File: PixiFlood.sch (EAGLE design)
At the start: 37 parts, among them IC1 TC7W04FP-0.65, IC2 WS2811S, IC3 78L05Z, U1 PT4115B89E, U2 PT4115B89E, U3 PT4115B89E, X1 22-23-2031, X2 22-23-2031

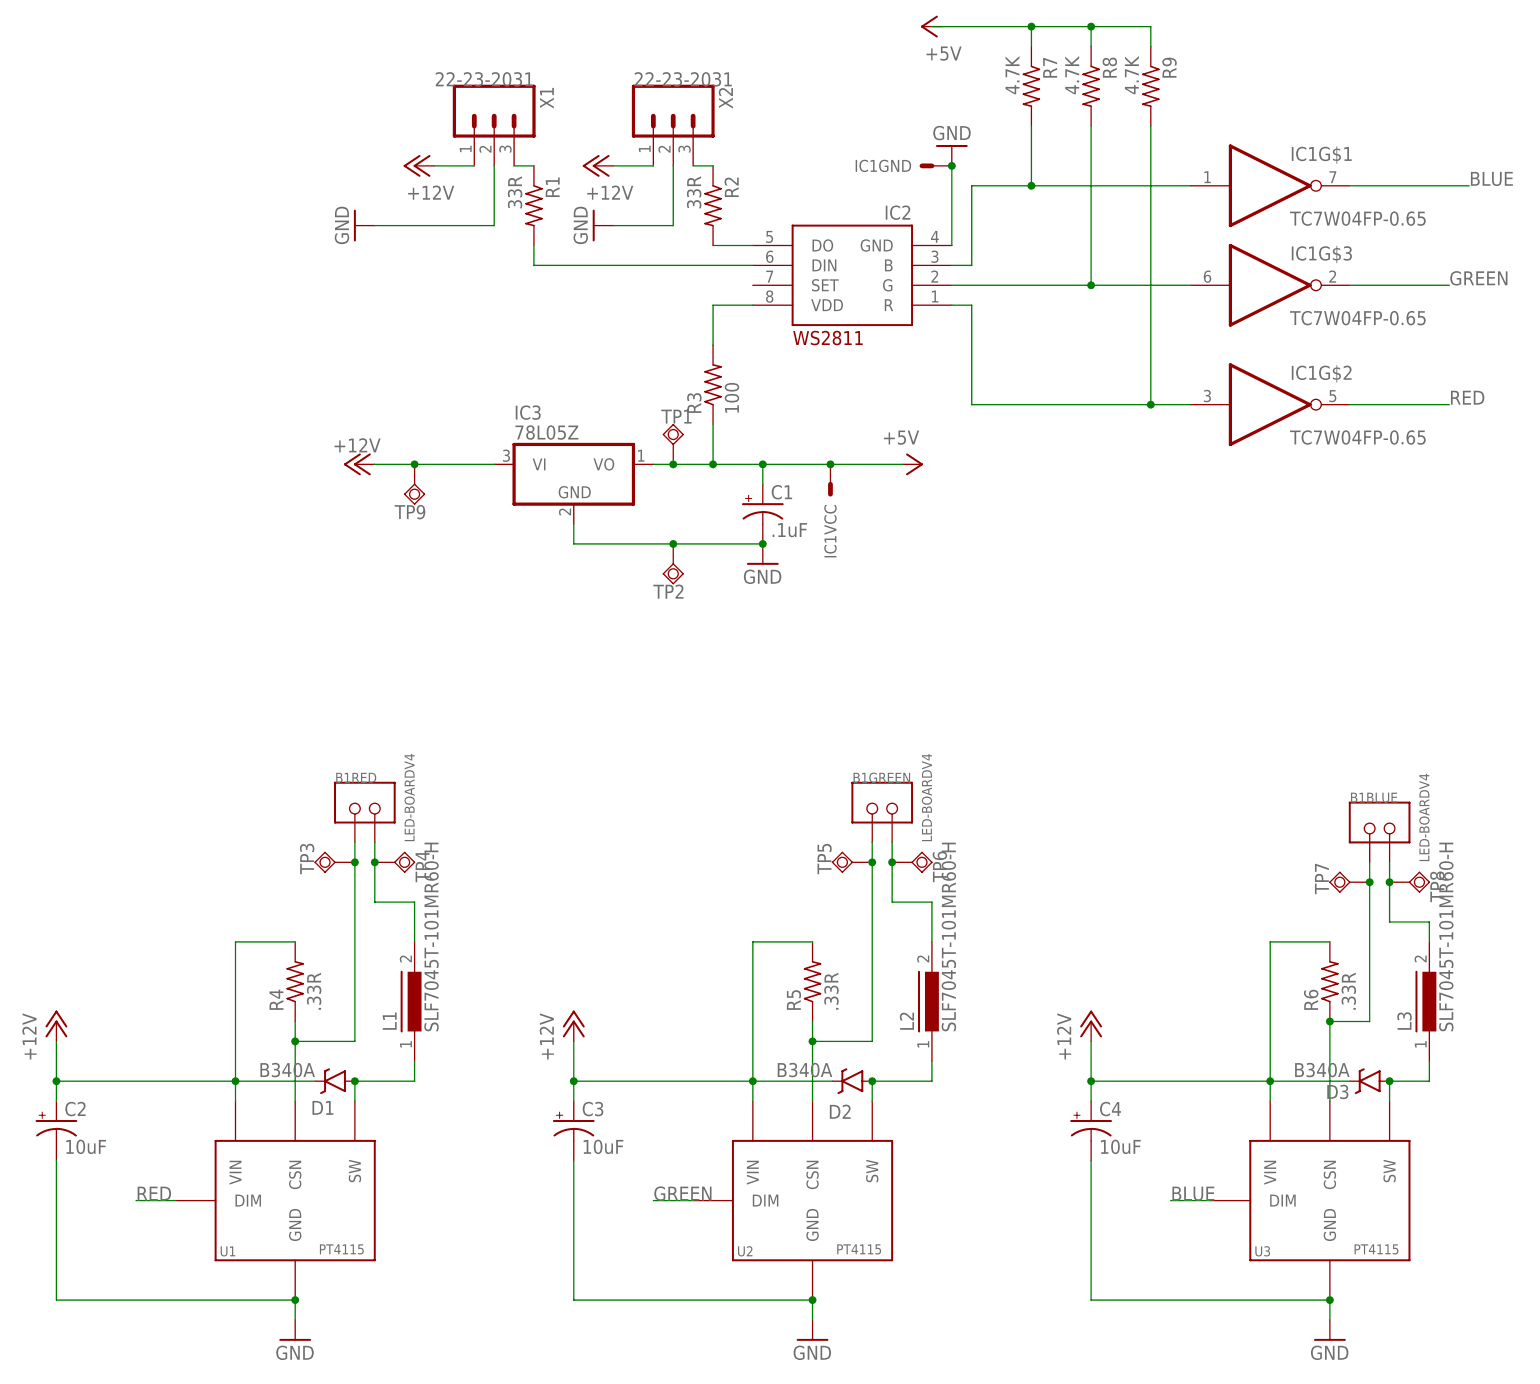
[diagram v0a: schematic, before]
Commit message: Reworked layout
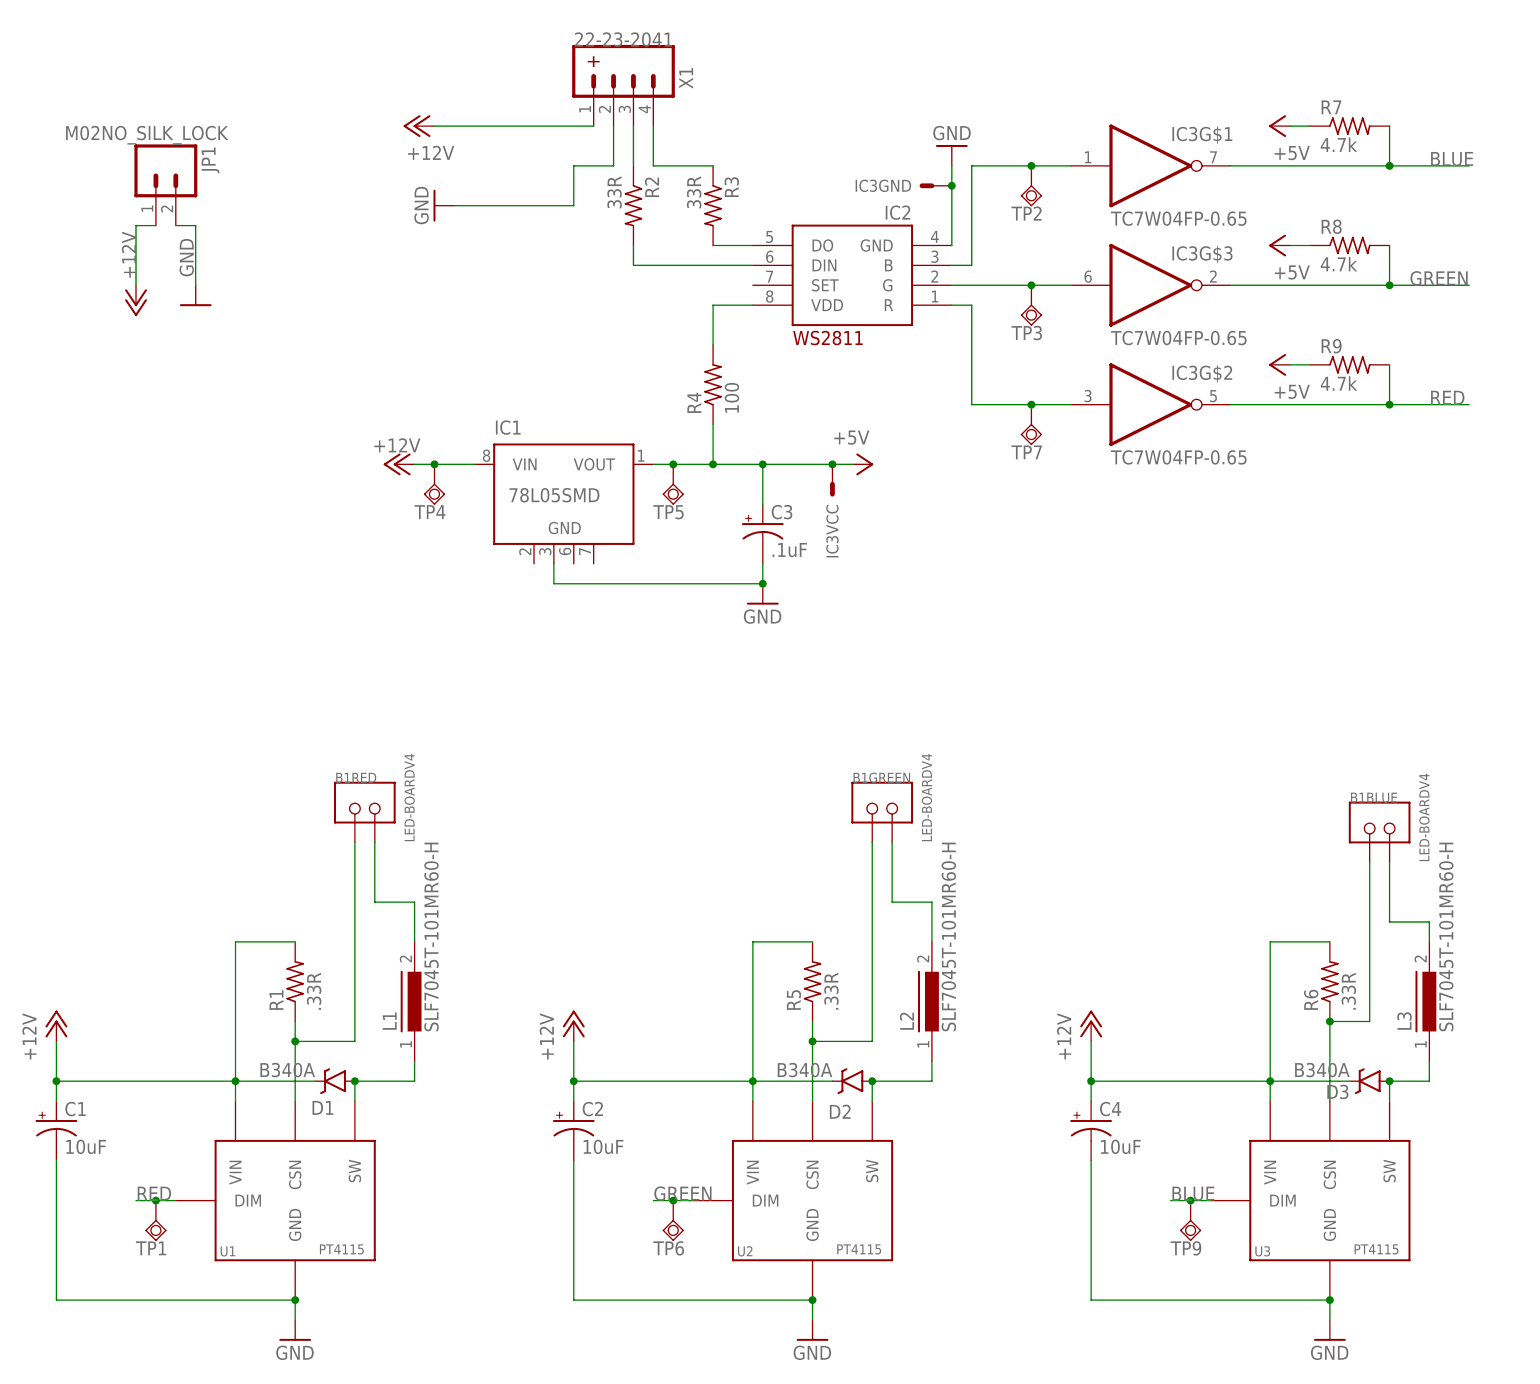
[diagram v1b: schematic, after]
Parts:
- removed TP8: TPSQTP15SQ, testpad:TPSQTP15SQ
- removed X2: 22-23-2031, MyLibrary:22-23-2031
- added JP1: M02NO_SILK_LOCK, connectors:M02NO_SILK_LOCK
- C1: value .1uF -> 10uF; device capacitors:CAP_POL1206 -> capacitors:CAP_POLCASE-D
- C3: value 10uF -> .1uF; device capacitors:CAP_POLCASE-D -> capacitors:CAP_POL1206
- IC1: value TC7W04FP-0.65 -> 78L05SMD; device logic:TC7W04FP-0.65 -> regulators:78L05SMD
- IC3: value 78L05Z -> TC7W04FP-0.65; device linear:78L05Z -> logic:TC7W04FP-0.65
- R1: value 33R -> .33R; device rcl:R-US_R1206 -> resistor:R-US_R1210
- R3: value 100 -> 33R
- R4: value .33R -> 100; device resistor:R-US_R1210 -> rcl:R-US_R1206
- R7, R8, R9: value 4.7K -> 4.7k; device rcl:R-US_R0805 -> rcl:R-US_R1206
- TP1: value TPSQTP20R -> TPSQTP15R; device testpad:TPSQTP20R -> testpad:TPSQTP15R
- TP2: value TPSQTP20SQ -> TPSQTP15R; device testpad:TPSQTP20SQ -> testpad:TPSQTP15R
- TP4, TP6: value TPSQTP15SQ -> TPSQTP15R; device testpad:TPSQTP15SQ -> testpad:TPSQTP15R
- U1, U2, U3: value PT4115B89E -> PT4115B89E-A; device drivers:PT4115B89E -> drivers:PT4115B89E-A
- X1: value 22-23-2031 -> 22-23-2041; device MyLibrary:22-23-2031 -> connectors:22-23-2041
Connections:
- removed net N$18: R7.1, R8.1, R9.1
- net +12V: now also C1.+, IC1G$1.VIN, JP1.1, R1.2, TP4.TP; no longer C3.+, IC3.VI, R4.2, TP9.TP, X2.1
- net +5V: now also C3.+, IC1G$1.VOUT, IC3VCC.S, R4.1, R7.1, R8.1, R9.1, TP5.TP; no longer C1.+, IC1VCC.S, IC3.VO, R3.1, TP1.TP
- net BLUE: now also IC3G$1.O, R7.2, TP9.TP; no longer IC1G$1.O
- net BOUT: no longer TP7.TP
- net GND: now also IC1G$1.GND@2, IC3GND.S, JP1.2; no longer IC1GND.S, IC3.GND, TP2.TP, X2.2
- net GOUT: no longer TP5.TP
- net GREEN: now also IC3G$3.O, R8.2, TP6.TP; no longer IC1G$3.O
- net N$10: no longer TP8.TP
- net N$14: now also R4.2; no longer R3.2
- net N$15: now also IC3G$2.I, TP7.TP; no longer IC1G$2.I, R9.2
- net N$16: now also IC3G$1.I, TP2.TP; no longer IC1G$1.I, R7.2
- net N$19: now also IC3G$3.I, TP3.TP; no longer IC1G$3.I, R8.2
- net N$3: no longer TP4.TP
- net N$4: now also R3.1, X1.4; no longer R2.1, X2.3
- net N$6: now also R2.1; no longer R1.1
- net N$7: now also R3.2; no longer R2.2
- net N$8: now also R2.2; no longer R1.2
- net N$9: no longer TP6.TP
- net RED: now also IC3G$2.O, R9.2, TP1.TP; no longer IC1G$2.O
- net ROUT: now also R1.1; no longer R4.1, TP3.TP
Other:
- moved on the sheet: C1, C2, C3, R1, R2, R3, R4, R7, R8, R9, TP1, TP2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

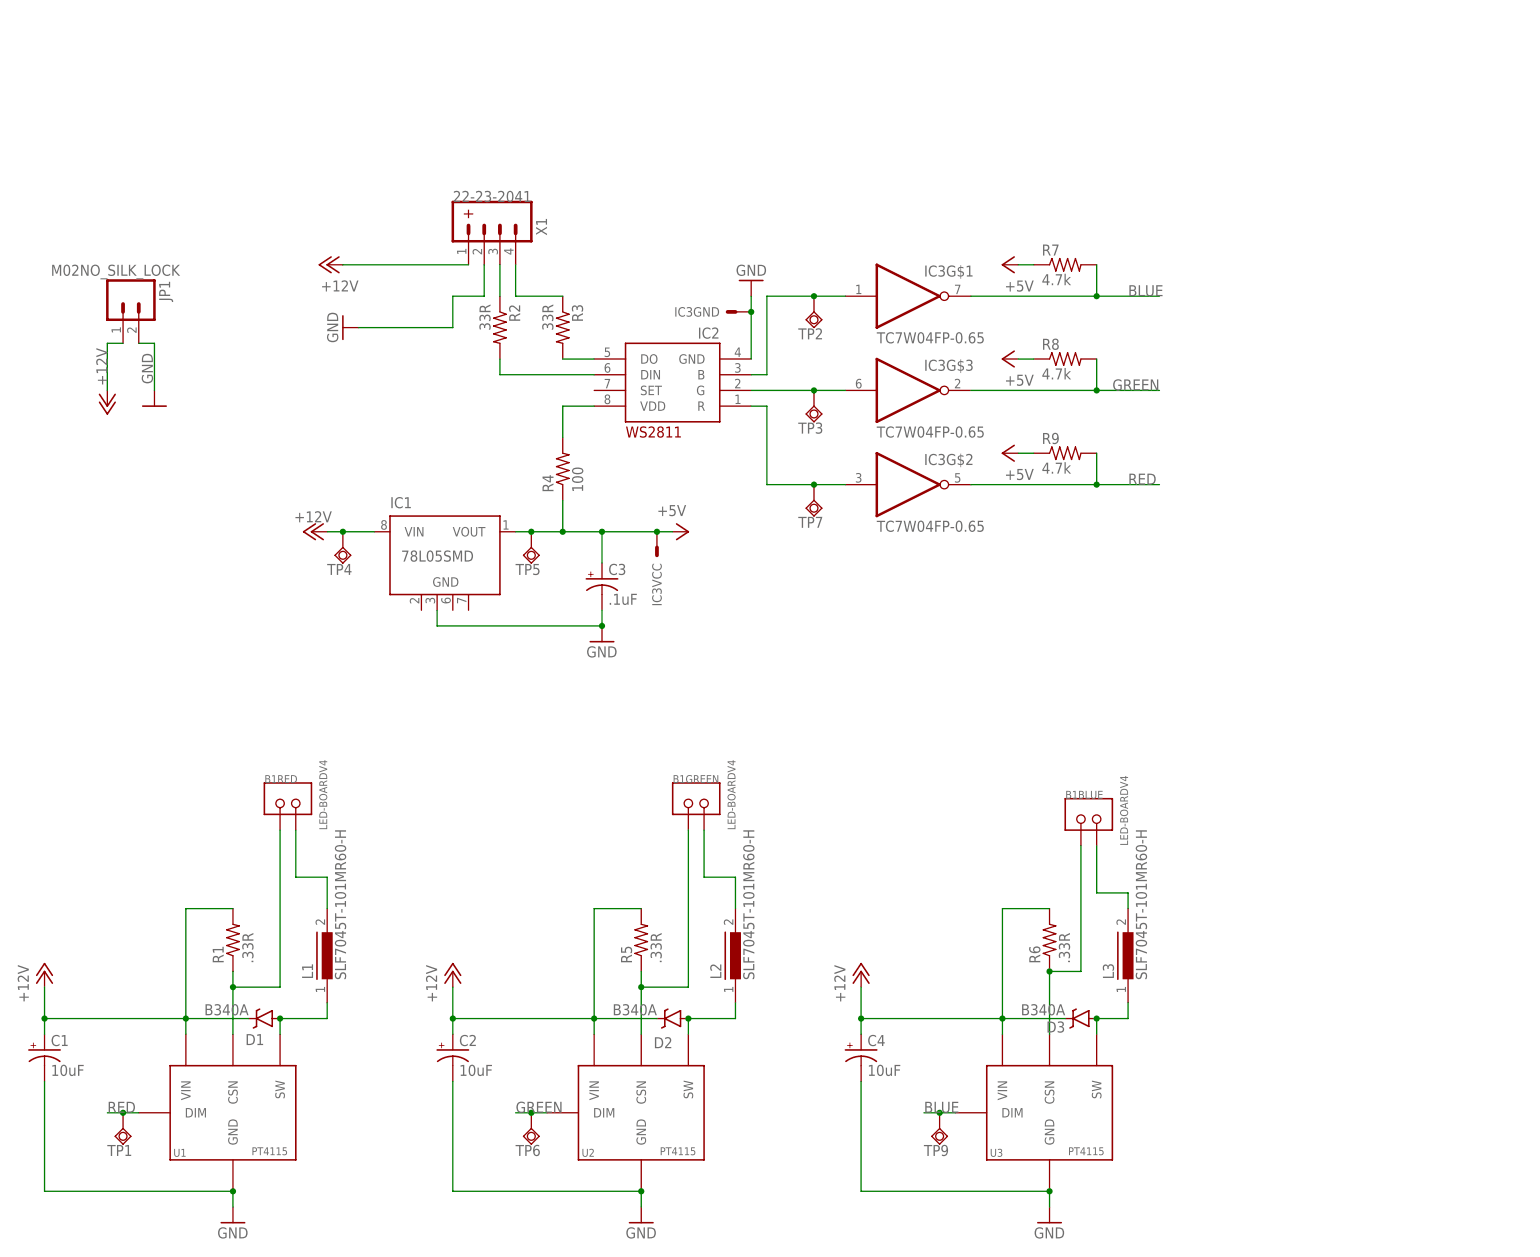
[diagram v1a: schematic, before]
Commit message: Reworked layout
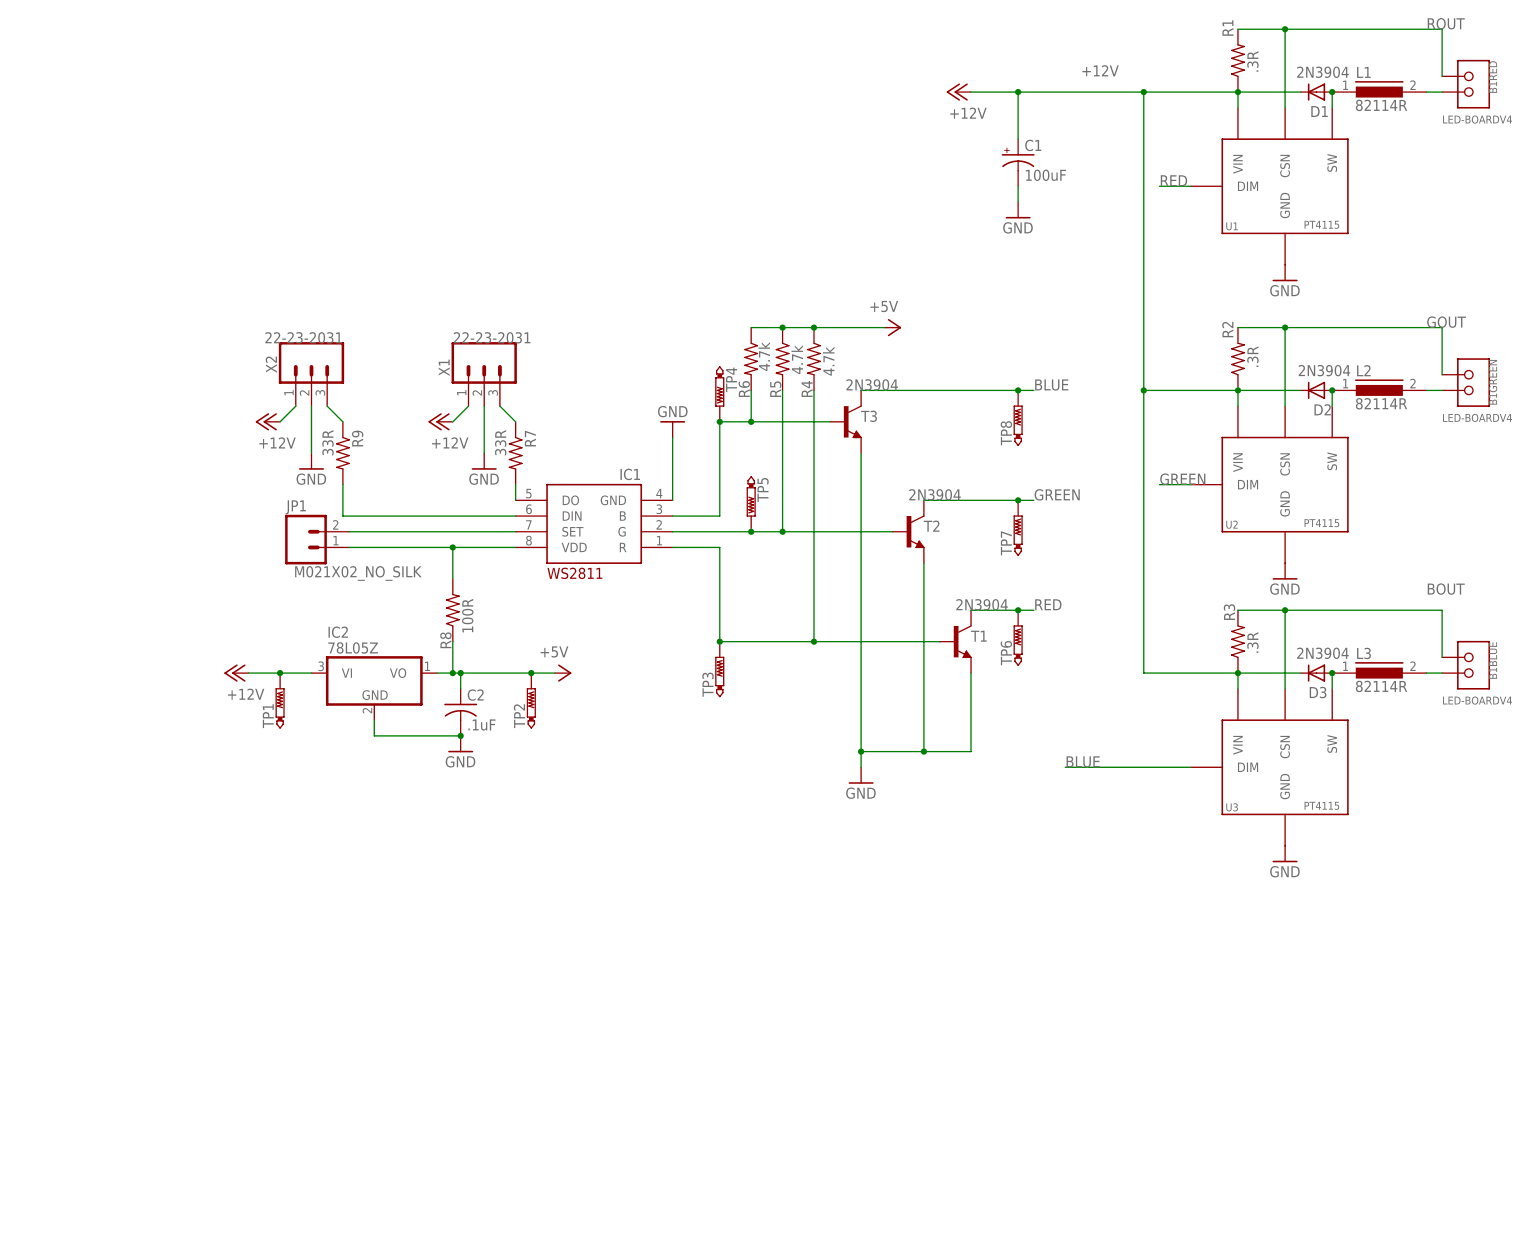
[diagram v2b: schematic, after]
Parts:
- removed C3: .1uF, capacitors:CAP_POL1206
- removed C4: 10uF, capacitors:CAP_POLCASE-D
- removed IC3: TC7W04FP-0.65, logic:TC7W04FP-0.65
- removed TP9: TPSQTP15R, testpad:TPSQTP15R
- added T1, T2, T3: 2N3904, transistor:2N3904
- added TP8: PTR1B1,27, testpad:PTR1B1,27
- added X2: 22-23-2031, connectors:22-23-2031
- C1: value 10uF -> 100uF; device capacitors:CAP_POLCASE-D -> rcl:CPOL-USTT2D6L
- C2: value 10uF -> .1uF; device capacitors:CAP_POLCASE-D -> rcl:C-US050-024X044
- D1, D2, D3: value B340A -> 2N3904; device SparkFun-DiscreteSemi:DIODE-SCHOTTKY-B340A -> diode:DIODE-DO07
- IC1: value 78L05SMD -> WS2811-SOP8; device regulators:78L05SMD -> MyLibrary:WS2811-SOP8
- IC2: value WS2811S -> 78L05Z; device drivers:WS2811S -> linear:78L05Z
- JP1: value M02NO_SILK_LOCK -> M021X02_NO_SILK; device connectors:M02NO_SILK_LOCK -> SparkFun-Connectors:M021X02_NO_SILK
- L1, L2, L3: value SLF7045T-101MR60-H -> 82114R; device inductors:SLF7045 -> inductors:82114R
- R1: value .33R -> .3R; device resistor:R-US_R1210 -> resistor:R-US_0204/7
- R2, R3: value 33R -> .3R; device rcl:R-US_R1206 -> resistor:R-US_0204/7
- R4: value 100 -> 4.7k; device rcl:R-US_R1206 -> resistor:R-US_0204/7
- R5, R6: value .33R -> 4.7k; device resistor:R-US_R1210 -> resistor:R-US_0204/7
- R7, R9: value 4.7k -> 33R; device rcl:R-US_R1206 -> rcl:R-US_0204/7
- R8: value 4.7k -> 100R; device rcl:R-US_R1206 -> rcl:R-US_0204/7
- TP1, TP2: value TPSQTP15R -> PTR1B2,54; device testpad:TPSQTP15R -> testpad:PTR1B2,54
- TP3, TP4, TP5, TP6, TP7: value TPSQTP15R -> PTR1B1,27; device testpad:TPSQTP15R -> testpad:PTR1B1,27
- U1, U2, U3: value PT4115B89E-A -> PT4115B89E-A2; device drivers:PT4115B89E-A -> drivers:PT4115B89E-A2
- X1: value 22-23-2041 -> 22-23-2031; device connectors:22-23-2041 -> connectors:22-23-2031
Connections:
- removed net N$14: IC2.VDD, R4.2
- removed net N$19: IC2.G, IC3G$3.I, TP3.TP
- new net N$18: IC1.G, R5.2, T2.B, TP5.TP
- new net N$20: IC1.R, R4.2, T1.B, TP3.TP
- new net VDD: IC1.VDD, JP1.1, R8.2
- net +12V: now also IC2.VI, R1.1, R2.1, R3.1, TP1.TP, X2.1; no longer C2.+, C4.+, IC1G$1.VIN, JP1.1, R1.2, R5.2, R6.2, TP4.TP
- net +5V: now also C2.1, IC2.VO, R5.1, R6.1, TP2.TP; no longer C3.+, IC1G$1.VOUT, IC3VCC.S, R7.1, R9.1, TP5.TP
- net BLUE: now also T3.C, TP8.TP; no longer IC3G$1.O, R7.2, TP9.TP
- net BOUT: now also R3.2; no longer R6.1
- net GND: now also C2.2, IC1.GND, T1.E, T2.E, T3.E, X2.2; no longer C2.-, C3.-, C4.-, IC1G$1.GND@2, IC3GND.S, JP1.2
- net GOUT: now also R2.2; no longer R5.1
- net GREEN: now also T2.C, TP7.TP; no longer IC3G$3.O, R8.2, TP6.TP
- net N$15: now also IC1.B, R6.2, T3.B, TP4.TP; no longer IC2.R, IC3G$2.I, TP7.TP
- net N$16: now also IC1.SET, JP1.2; no longer IC2.B, IC3G$1.I, TP2.TP
- net N$4: now also R7.1, X1.3; no longer R3.1, X1.4
- net N$6: now also R9.1, X2.3; no longer R2.1, X1.3
- net N$7: now also IC1.DO, R7.2; no longer IC2.DO, R3.2
- net N$8: now also IC1.DIN, R9.2; no longer IC2.DIN, R2.2
- net RED: now also T1.C, TP6.TP; no longer IC3G$2.O, R9.2, TP1.TP
- net ROUT: now also R1.2; no longer R1.1
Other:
- moved on the sheet: B1BLUE, B1GREEN, B1RED, C1, JP1, R1, R2, R3, R4, R5, R6, R7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
